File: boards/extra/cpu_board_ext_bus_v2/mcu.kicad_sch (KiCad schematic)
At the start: 8 parts, among them U1 Z80CPPLC44, U2 GAL16V8, U3 74LS244, U4 74LS244, U5 74LS245, U6 74LS244

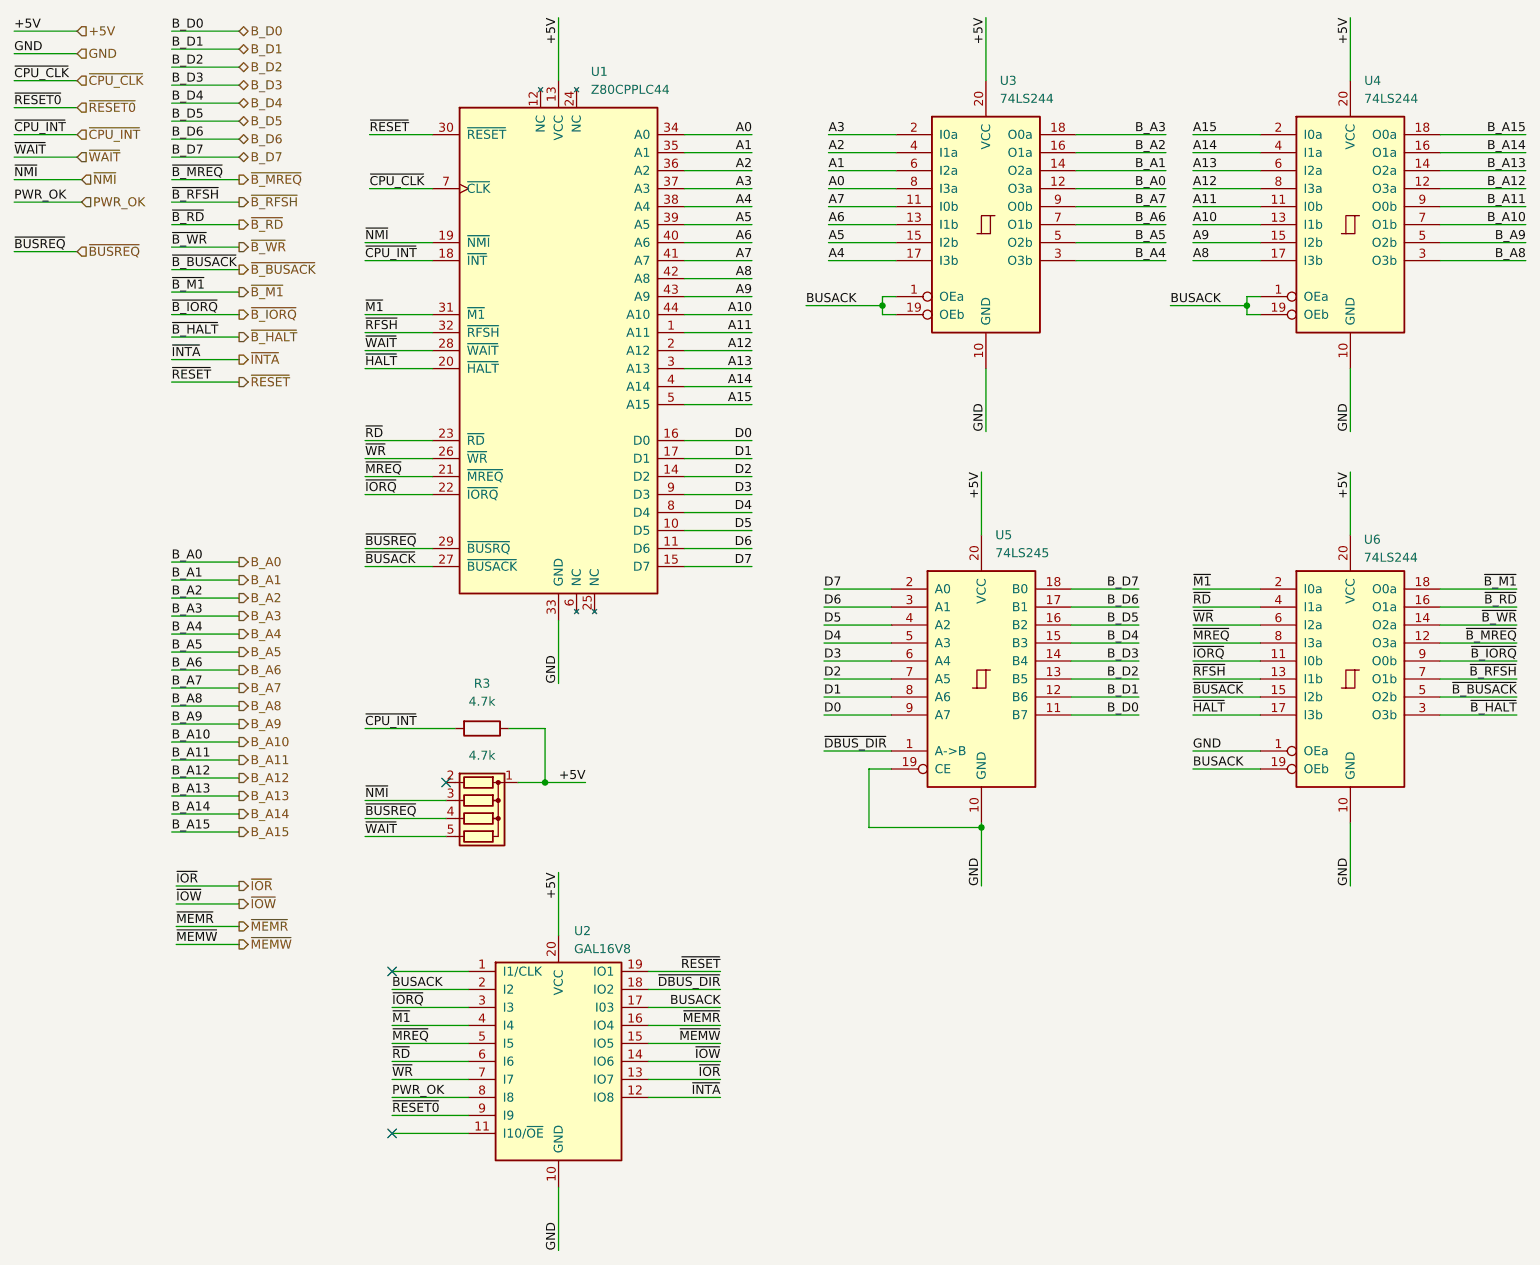
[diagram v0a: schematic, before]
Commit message: Updated CPU board V2 with extension bus
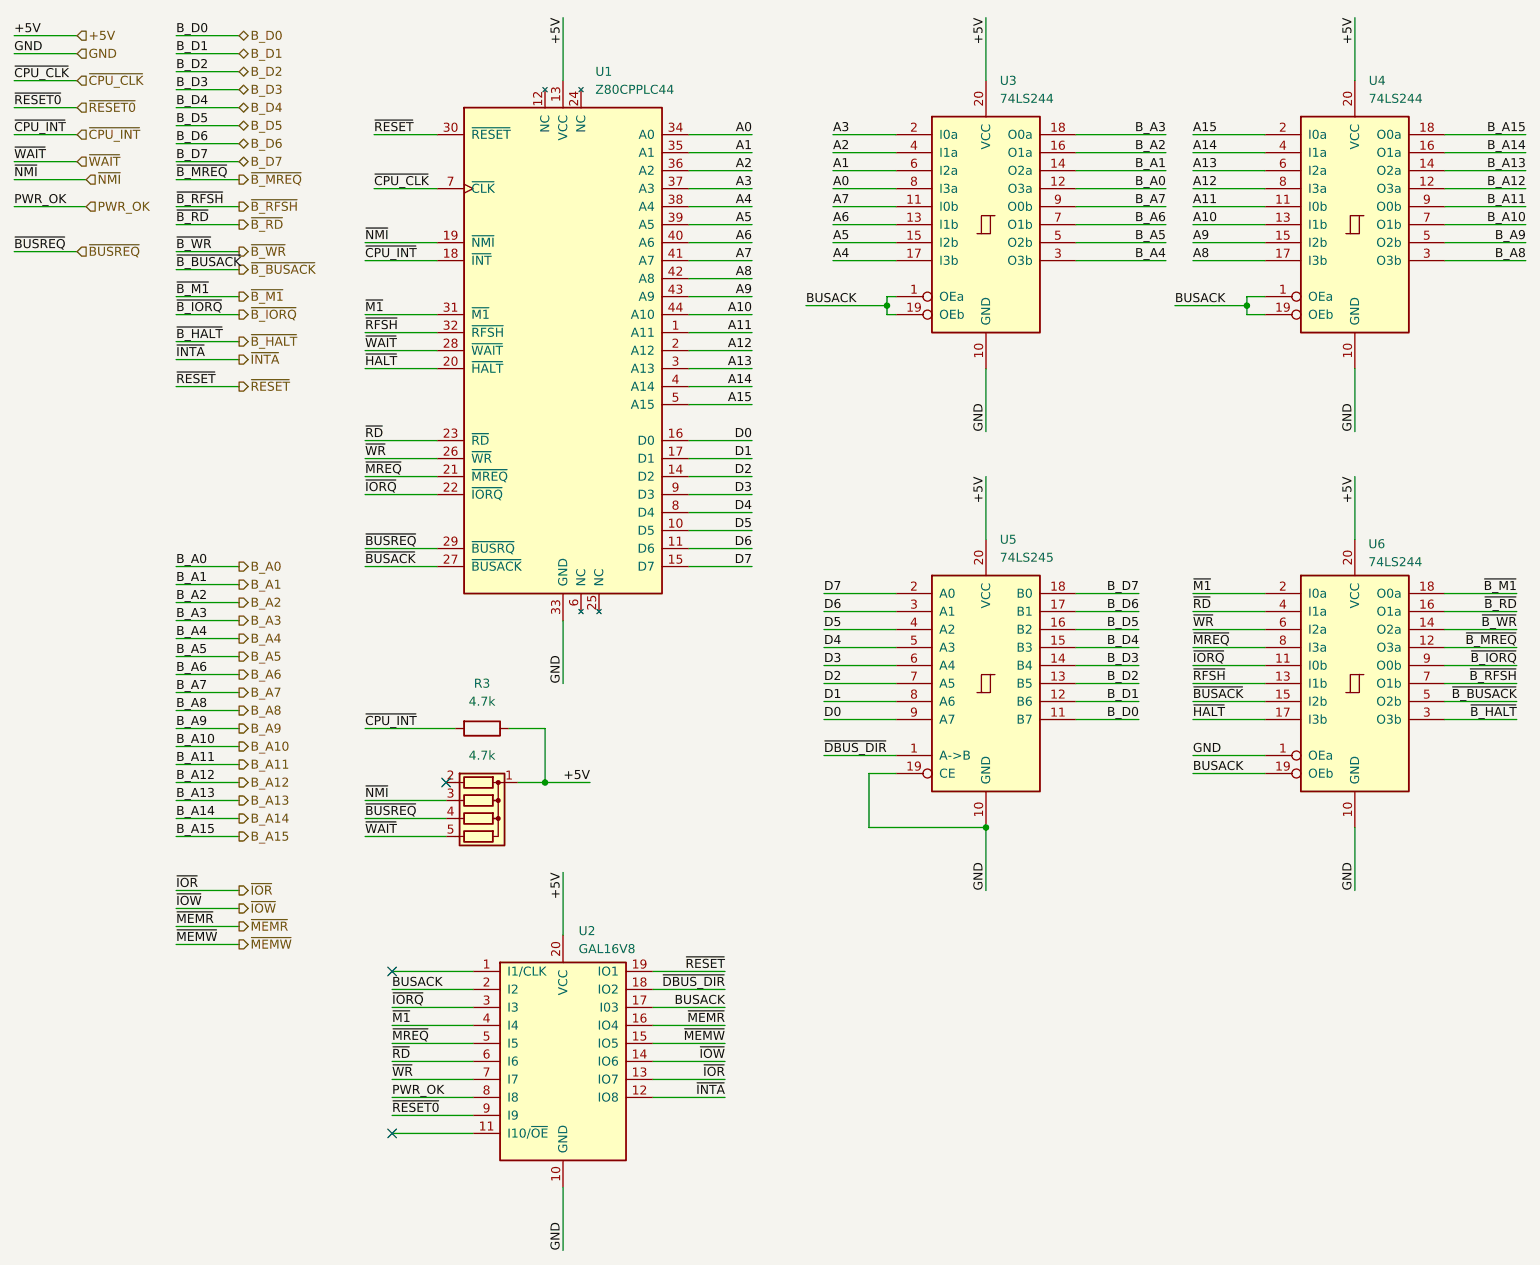
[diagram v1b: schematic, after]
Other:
- moved on the sheet: U1, U2, U4, U5, U6

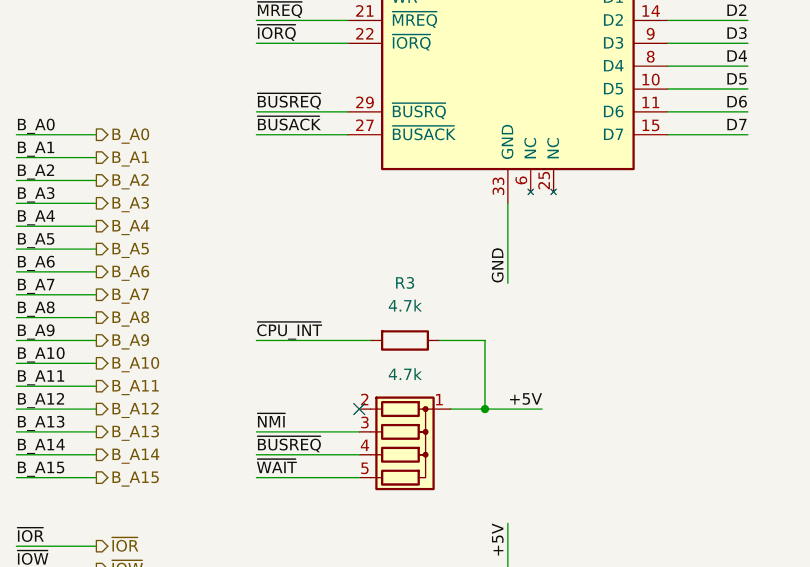
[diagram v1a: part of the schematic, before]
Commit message: Extended CPU board update
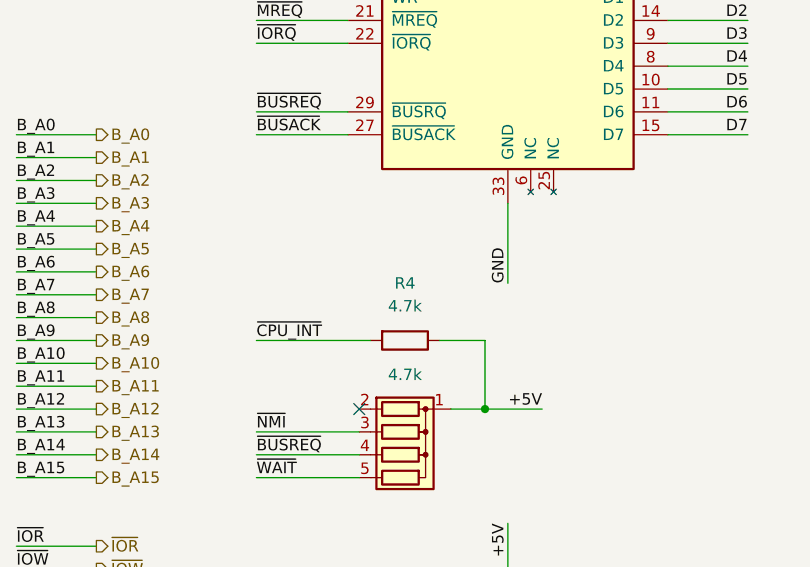
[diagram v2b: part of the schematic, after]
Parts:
- renumbered R3 to R4
